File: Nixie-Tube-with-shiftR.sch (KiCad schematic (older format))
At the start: 55 parts, among them J1 Conn_01x05_Male, J2 Conn_01x01_Female, J3 Conn_01x05_Female, J4 Conn_01x01_Male, Q1 MMBTA42LT1, Q10 MMBTA42LT1, Q11 AO3400, Q12 AO3400, Q13 AO3400, Q14 MMBTA42LT1, Q15 MMBTA42LT1, Q2 MMBTA42LT1, Q3 MMBTA42LT1, Q4 MMBTA42LT1, Q5 MMBTA42LT1, Q6 MMBTA42LT1, Q7 MMBTA42LT1, Q8 MMBTA42LT1, Q9 MMBTA42LT1, U1 74HC595D, U3 74HC595D, U4 ams1117-5.0

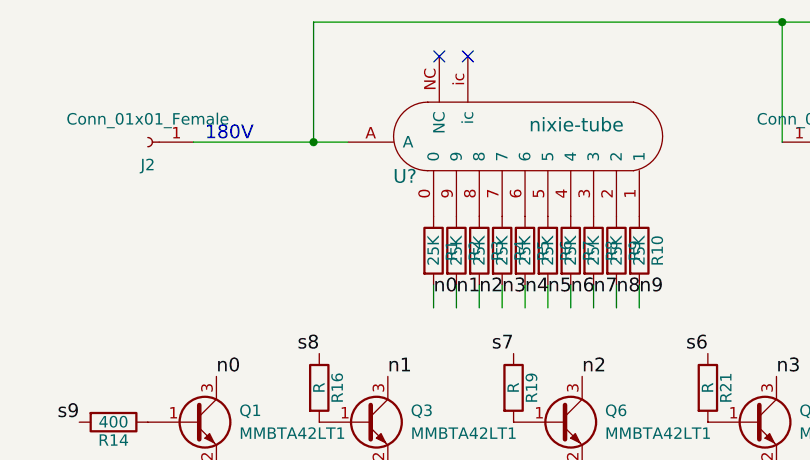
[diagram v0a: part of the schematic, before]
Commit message: place group(cap and R) parallel to the R, unite the track to nixie to 1 side
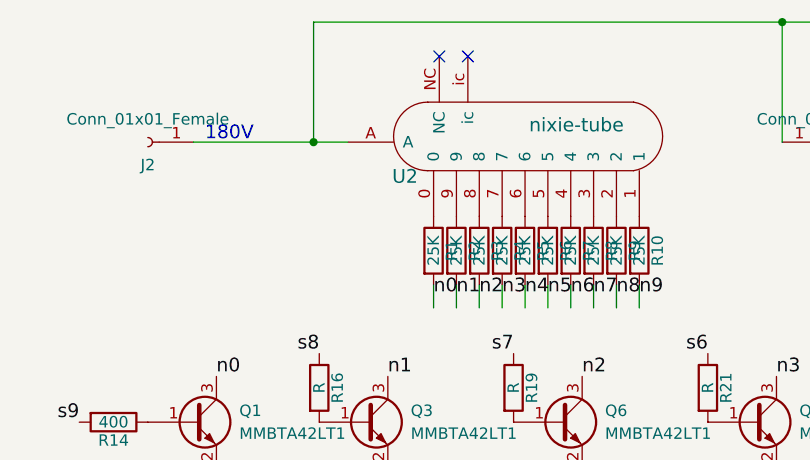
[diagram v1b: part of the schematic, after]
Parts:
- gave numbers to parts that had none: 1
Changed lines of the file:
@@
 DotD
 $Comp
-L nixie-tube U?
+L nixie-tube U2
 U 1 1 59E3559F
 P 5450 1950
-F 0 "U?" H 4875 2050 60  0000 C CNN
+F 0 "U2" H 4875 2050 60  0000 C CNN
 F 1 "nixie-tube" H 5625 2275 60  0000 C CNN
 F 2 "nixie-tube-fp:qs30-1" H 5150 1975 60  0001 C CNN

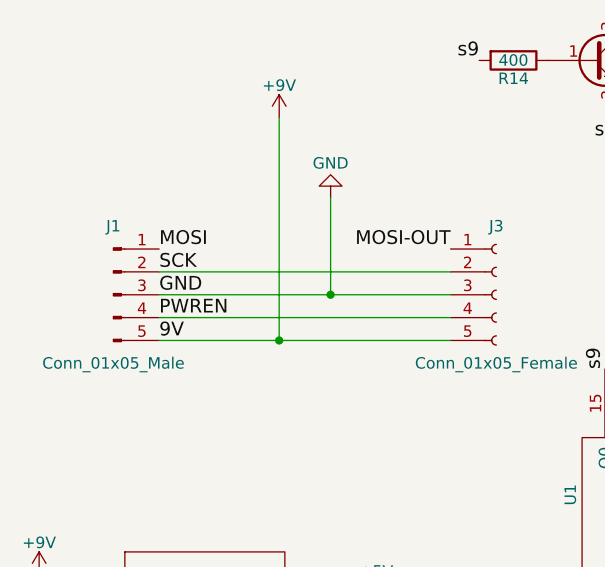
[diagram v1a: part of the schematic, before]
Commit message: completed routing, swap pin headers
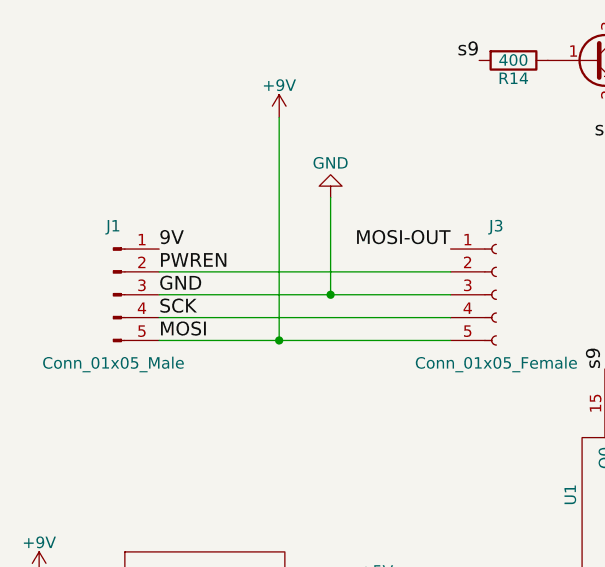
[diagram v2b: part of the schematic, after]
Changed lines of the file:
@@
 	-1   0    0    1
 $EndComp
-Text Label 2050 3750 0    60   ~ 0
+Text Label 2050 4150 0    60   ~ 0
 MOSI
-Text Label 2050 3850 0    60   ~ 0
+Text Label 2050 4050 0    60   ~ 0
 SCK
 Text Label 2050 3950 0    60   ~ 0
 GND
-Text Label 2050 4050 0    60   ~ 0
+Text Label 2050 3850 0    60   ~ 0
 PWREN
-Text Label 2050 4150 0    60   ~ 0
+Text Label 2050 3750 0    60   ~ 0
 9V
 $Comp

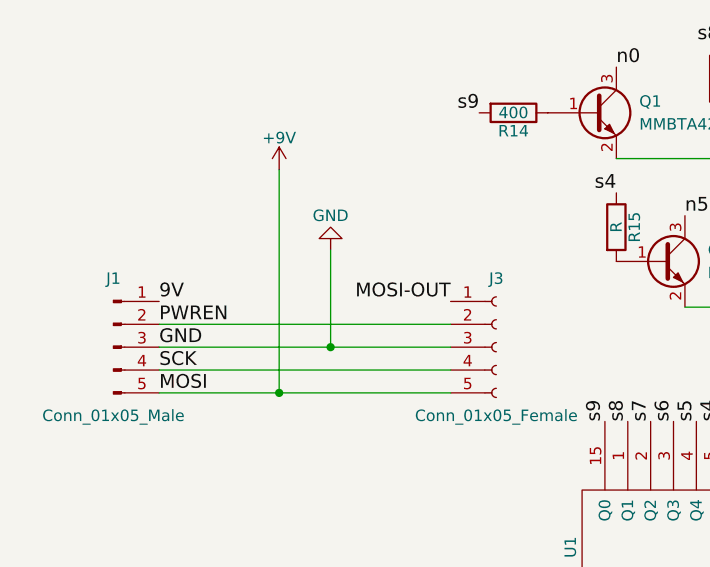
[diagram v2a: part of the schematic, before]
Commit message: mosi line bugged
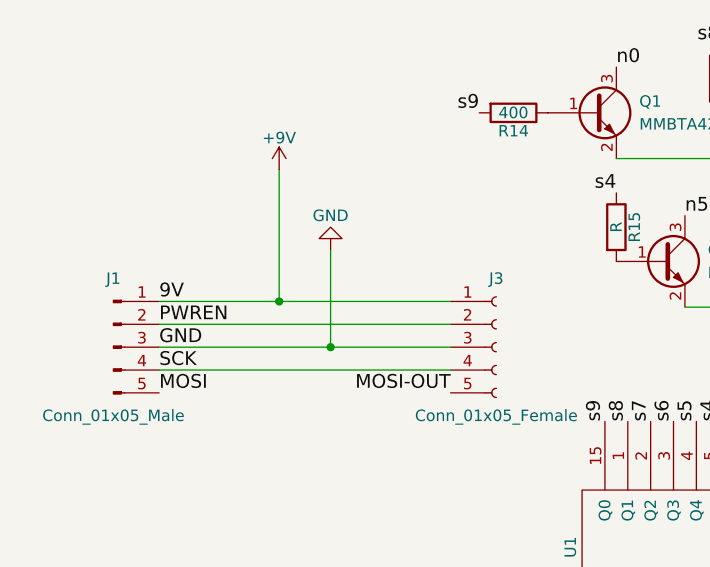
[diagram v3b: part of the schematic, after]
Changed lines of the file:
@@
 	3325 4050 2050 4050
 Wire Wire Line
-	2050 4150 3325 4150
-Wire Wire Line
 	4900 4275 5325 4275
 Wire Wire Line
@@
 Wire Wire Line
 	5625 5700 5625 5650
-Text Label 3325 3750 2    60   ~ 0
+Text Label 3325 4150 2    60   ~ 0
 MOSI-OUT
 Text Label 6525 4250 1    60   ~ 0
@@
 	1    0    0    -1
 $EndComp
-Wire Wire Line
-	2575 3175 2575 4150
-Connection ~ 2575 4150
 $Comp
 L GND #PWR08
@@
 NoConn ~ 5025 1325
 NoConn ~ 5150 1325
+Wire Wire Line
+	2050 3750 3325 3750
+Wire Wire Line
+	2575 3175 2575 3750
+Connection ~ 2575 3750
 $EndSCHEMATC

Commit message: finalize board layout and tracks
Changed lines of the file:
@@
 	-1   0    0    1
 $EndComp
-Text Label 2050 4150 0    60   ~ 0
+Text Label 3325 4150 2    60   ~ 0
 MOSI
 Text Label 2050 4050 0    60   ~ 0
@@
 Wire Wire Line
 	5625 5700 5625 5650
-Text Label 3325 4150 2    60   ~ 0
+Text Label 2050 4150 0    60   ~ 0
 MOSI-OUT
 Text Label 6525 4250 1    60   ~ 0

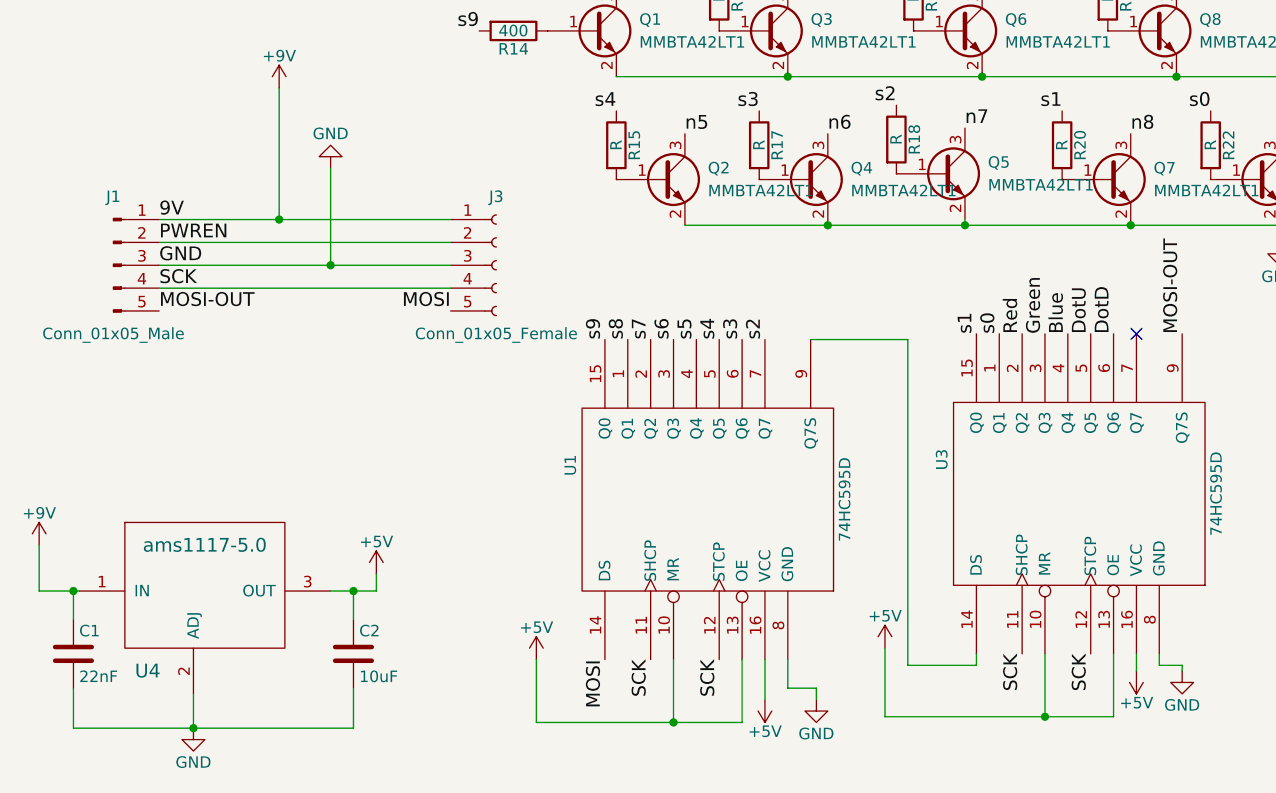
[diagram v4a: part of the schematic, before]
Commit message: added OE to the pins
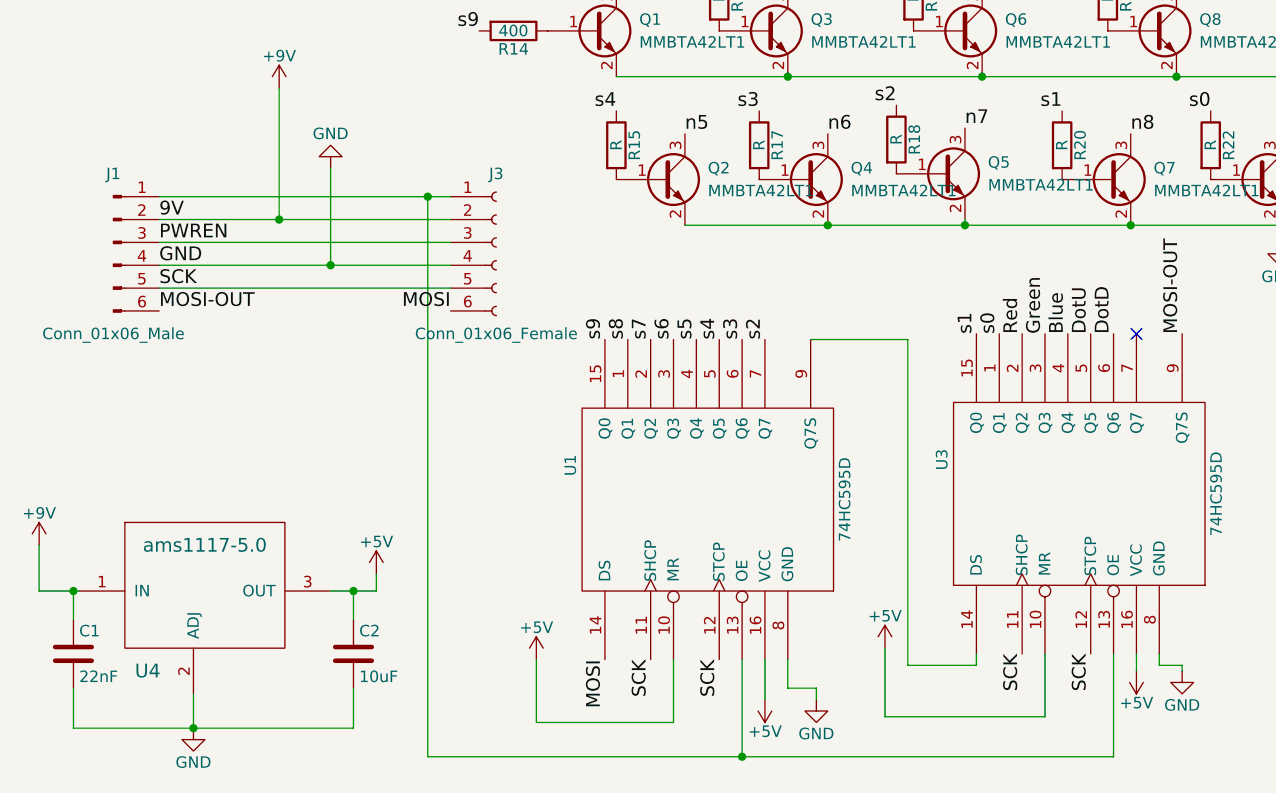
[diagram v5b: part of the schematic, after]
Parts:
- removed J1: Conn_01x05_Male, Pin_Headers:Pin_Header_Angled_1x05_Pitch2.54mm, symbol Conn_01x05_Male
- removed J3: Conn_01x05_Female, Socket_Strips:Socket_Strip_Angled_1x05_Pitch2.54mm, symbol Conn_01x05_Female
- added J1: Conn_01x06_Male, Pin_Headers:Pin_Header_Angled_1x06_Pitch2.54mm, symbol Conn_01x06_Male
- added J3: Conn_01x06_Female, Socket_Strips:Socket_Strip_Angled_1x06_Pitch2.54mm, symbol Conn_01x06_Female
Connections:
- wire segments 63 -> 66
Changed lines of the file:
@@
 Text Label 2050 3750 0    60   ~ 0
 9V
-$Comp
-L Conn_01x05_Female J3
-U 1 1 59DFF03E
-P 3525 3950
-F 0 "J3" H 3525 4250 50  0000 C CNN
-F 1 "Conn_01x05_Female" H 3525 3650 50  0000 C CNN
-F 2 "Socket_Strips:Socket_Strip_Angled_1x05_Pitch2.54mm" H 3525 3950 50  0001 C CNN
-F 3 "" H 3525 3950 50  0001 C CNN
-	1    3525 3950
-	1    0    0    -1
-$EndComp
-$Comp
-L Conn_01x05_Male J1
-U 1 1 59DFF2D1
-P 1850 3950
-F 0 "J1" H 1850 4250 50  0000 C CNN
-F 1 "Conn_01x05_Male" H 1850 3650 50  0000 C CNN
-F 2 "Pin_Headers:Pin_Header_Angled_1x05_Pitch2.54mm" H 1850 3950 50  0001 C CNN
-F 3 "" H 1850 3950 50  0001 C CNN
-	1    1850 3950
-	1    0    0    -1
-$EndComp
 Wire Wire Line
 	2050 3850 3325 3850
@@
 	4300 5675 4300 5950
 Wire Wire Line
-	3700 5950 4600 5950
-Wire Wire Line
 	3700 5950 3700 5675
 Wire Wire Line
 	5925 5650 5925 5925
 Wire Wire Line
-	5225 5925 6225 5925
-Wire Wire Line
 	5225 5925 5225 5625
-Wire Wire Line
-	4600 5950 4600 5675
-Connection ~ 4300 5950
-Wire Wire Line
-	6225 5925 6225 5650
-Connection ~ 5925 5925
 $Comp
 L +9V #PWR07
@@
 	2575 3175 2575 3750
 Connection ~ 2575 3750
+$Comp
+L Conn_01x06_Male J1
+U 1 1 59EA0627
+P 1850 3850
+F 0 "J1" H 1850 4150 50  0000 C CNN
+F 1 "Conn_01x06_Male" H 1850 3450 50  0000 C CNN
+F 2 "Pin_Headers:Pin_Header_Angled_1x06_Pitch2.54mm" H 1850 3850 50  0001 C CNN
+F 3 "" H 1850 3850 50  0001 C CNN
+	1    1850 3850
+	1    0    0    -1
+$EndComp
+$Comp
+L Conn_01x06_Female J3
+U 1 1 59EA0C3B
+P 3525 3850
+F 0 "J3" H 3525 4150 50  0000 C CNN
+F 1 "Conn_01x06_Female" H 3525 3450 50  0000 C CNN
+F 2 "Socket_Strips:Socket_Strip_Angled_1x06_Pitch2.54mm" H 3525 3850 50  0001 C CNN
+F 3 "" H 3525 3850 50  0001 C CNN
+	1    3525 3850
+	1    0    0    -1
+$EndComp
+Wire Wire Line
+	4300 5950 3700 5950
+Wire Wire Line
+	5925 5925 5225 5925
+Wire Wire Line
+	6225 5650 6225 6100
+Wire Wire Line
+	6225 6100 3225 6100
+Wire Wire Line
+	3225 6100 3225 3650
+Wire Wire Line
+	4600 5675 4600 6100
+Connection ~ 4600 6100
+Wire Wire Line
+	2050 3650 3325 3650
+Connection ~ 3225 3650
 $EndSCHEMATC

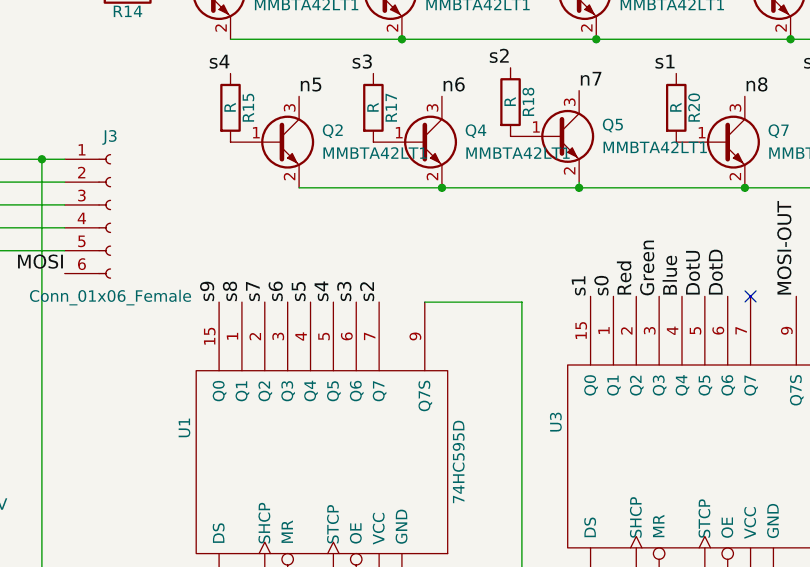
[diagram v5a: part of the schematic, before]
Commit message: change the sequence of s0-s9
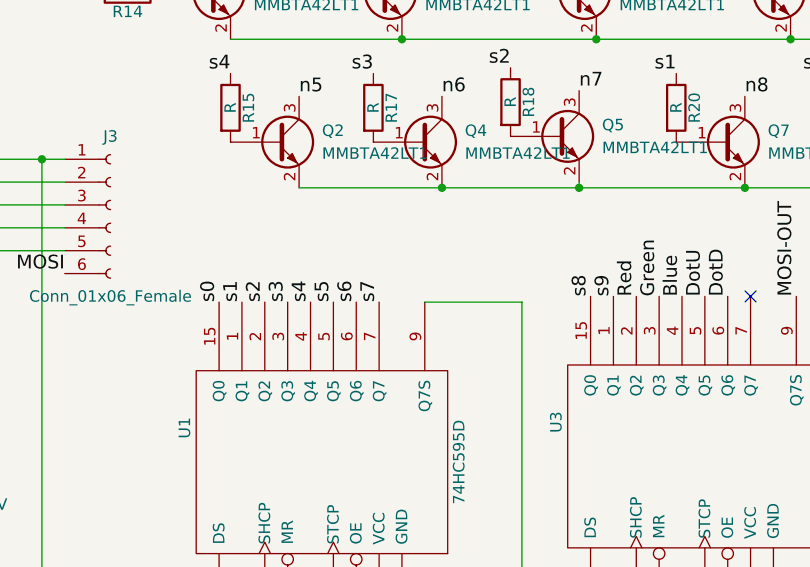
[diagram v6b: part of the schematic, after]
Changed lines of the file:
@@
 	1    0    0    -1
 $EndComp
-Text Label 4000 4275 1    60   ~ 0
+Text Label 5725 4250 1    60   ~ 0
 s9
+Text Label 5625 4250 1    60   ~ 0
+s8
+Text Label 4700 4275 1    60   ~ 0
+s7
+Text Label 4600 4275 1    60   ~ 0
+s6
+Text Label 4500 4275 1    60   ~ 0
+s5
+Text Label 4400 4275 1    60   ~ 0
+s4
+Text Label 4300 4275 1    60   ~ 0
+s3
+Text Label 4200 4275 1    60   ~ 0
+s2
 Text Label 4100 4275 1    60   ~ 0
-s8
-Text Label 4200 4275 1    60   ~ 0
-s7
-Text Label 4300 4275 1    60   ~ 0
-s6
-Text Label 4400 4275 1    60   ~ 0
-s5
-Text Label 4500 4275 1    60   ~ 0
-s4
-Text Label 4600 4275 1    60   ~ 0
-s3
-Text Label 4700 4275 1    60   ~ 0
-s2
-Text Label 5625 4250 1    60   ~ 0
 s1
 Wire Wire Line
@@
 Text Label 6650 3275 2    60   ~ 0
 s0
-Text Label 5725 4250 1    60   ~ 0
+Text Label 4000 4275 1    60   ~ 0
 s0
 $Comp

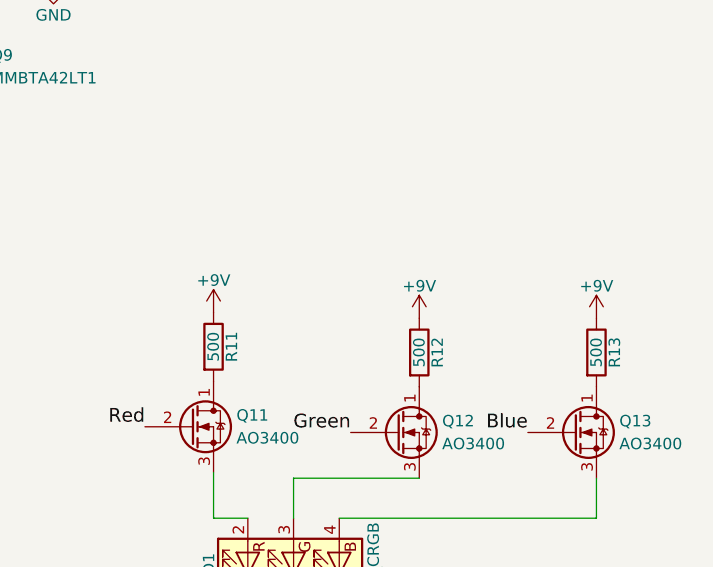
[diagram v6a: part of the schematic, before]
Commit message: finalized position, briefly routed
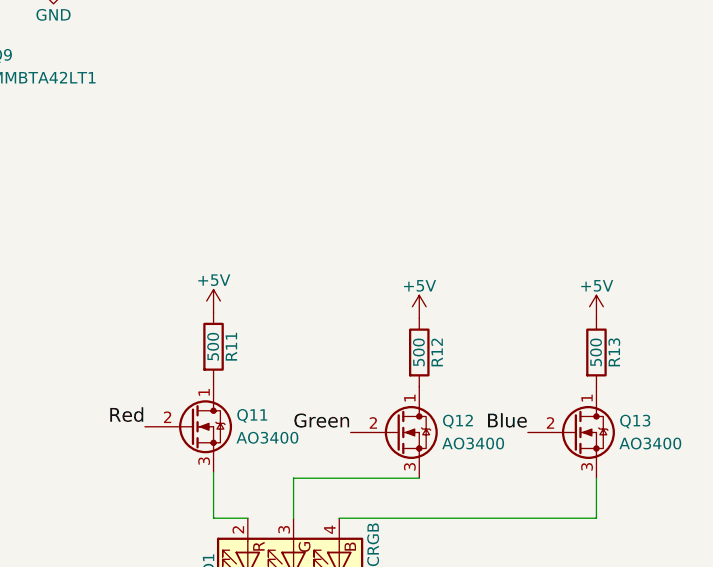
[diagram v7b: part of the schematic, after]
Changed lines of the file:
@@
 	2800 3950 2800 3525
 Connection ~ 2800 3950
-$Comp
-L +9V #PWR09
-U 1 1 59E08805
-P 8025 4650
-F 0 "#PWR09" H 8025 4500 50  0001 C CNN
-F 1 "+9V" H 8025 4790 50  0000 C CNN
-F 2 "" H 8025 4650 50  0001 C CNN
-F 3 "" H 8025 4650 50  0001 C CNN
-	1    8025 4650
-	1    0    0    -1
-$EndComp
-$Comp
-L +9V #PWR010
-U 1 1 59E088D3
-P 8925 4675
-F 0 "#PWR010" H 8925 4525 50  0001 C CNN
-F 1 "+9V" H 8925 4815 50  0000 C CNN
-F 2 "" H 8925 4675 50  0001 C CNN
-F 3 "" H 8925 4675 50  0001 C CNN
-	1    8925 4675
-	1    0    0    -1
-$EndComp
-$Comp
-L +9V #PWR011
-U 1 1 59E0896B
-P 9700 4675
-F 0 "#PWR011" H 9700 4525 50  0001 C CNN
-F 1 "+9V" H 9700 4815 50  0000 C CNN
-F 2 "" H 9700 4675 50  0001 C CNN
-F 3 "" H 9700 4675 50  0001 C CNN
-	1    9700 4675
-	1    0    0    -1
-$EndComp
 Text Label 5000 2375 0    60   ~ 0
 n0
@@
 	2050 3650 3325 3650
 Connection ~ 3225 3650
+$Comp
+L +5V #PWR?
+U 1 1 59EE23C2
+P 8025 4650
+F 0 "#PWR?" H 8025 4500 50  0001 C CNN
+F 1 "+5V" H 8025 4790 50  0000 C CNN
+F 2 "" H 8025 4650 50  0001 C CNN
+F 3 "" H 8025 4650 50  0001 C CNN
+	1    8025 4650
+	1    0    0    -1
+$EndComp
+$Comp
+L +5V #PWR?
+U 1 1 59EE25D6
+P 8925 4675
+F 0 "#PWR?" H 8925 4525 50  0001 C CNN
+F 1 "+5V" H 8925 4815 50  0000 C CNN
+F 2 "" H 8925 4675 50  0001 C CNN
+F 3 "" H 8925 4675 50  0001 C CNN
+	1    8925 4675
+	1    0    0    -1
+$EndComp
+$Comp
+L +5V #PWR?
+U 1 1 59EE2686
+P 9700 4675
+F 0 "#PWR?" H 9700 4525 50  0001 C CNN
+F 1 "+5V" H 9700 4815 50  0000 C CNN
+F 2 "" H 9700 4675 50  0001 C CNN
+F 3 "" H 9700 4675 50  0001 C CNN
+	1    9700 4675
+	1    0    0    -1
+$EndComp
 $EndSCHEMATC

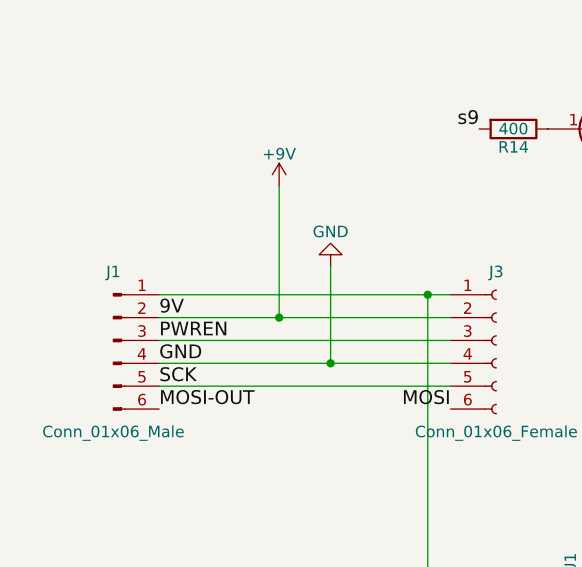
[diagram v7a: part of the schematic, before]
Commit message: fixed pin headers placement not the same with power supply
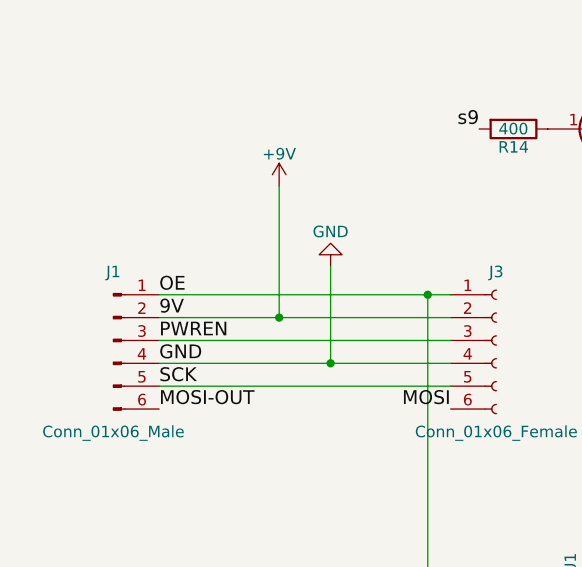
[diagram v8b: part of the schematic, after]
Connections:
- net labels added: OE
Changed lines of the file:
@@
 	1    0    0    -1
 $EndComp
+Text Label 2050 3650 0    60   ~ 0
+OE
 $EndSCHEMATC
